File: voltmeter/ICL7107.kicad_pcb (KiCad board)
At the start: 2 copper layers, 88.9 x 68.6 mm, 42 parts, among them J1 +9...12V DC, J2 DP conn., J3 meas. conn, M1 M2.2, M2 M2.2, M3 M2.2, M4 M2.2, U1 LM285Z-1.2, U2 ICL7107, U3 L7805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

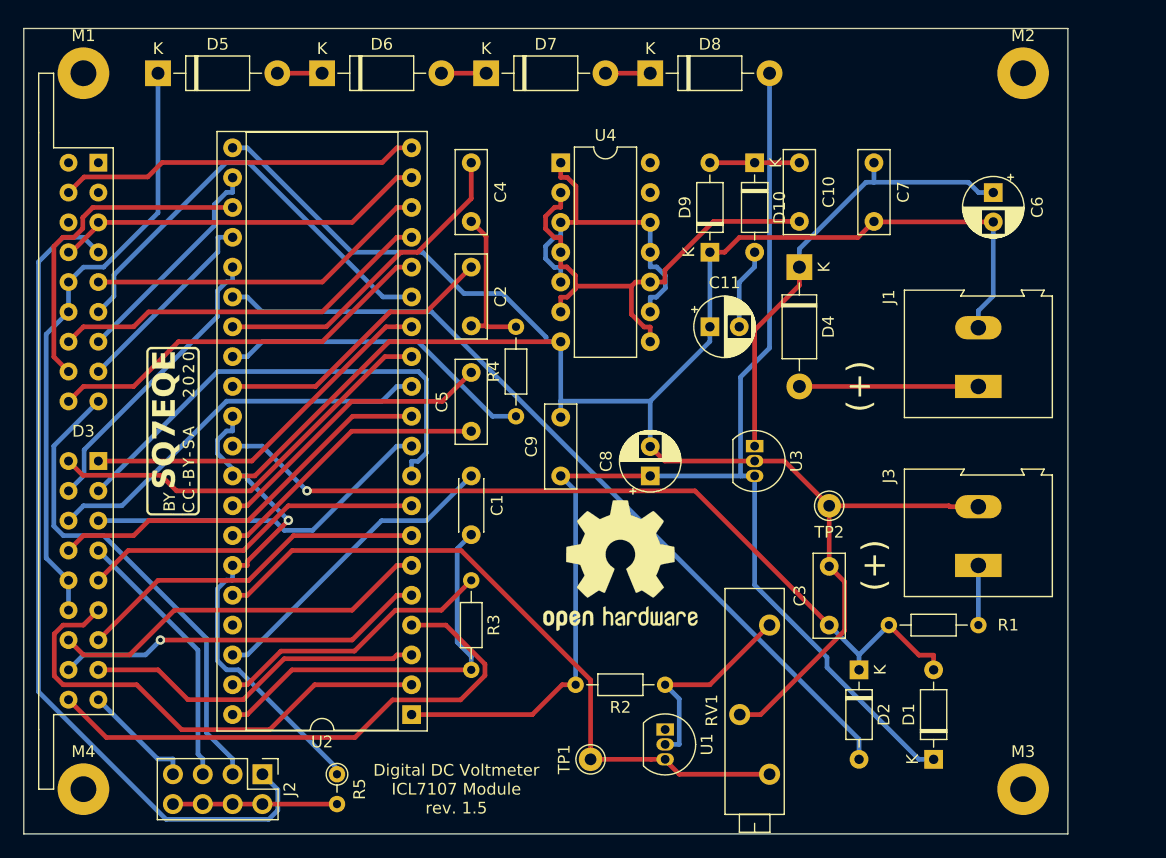
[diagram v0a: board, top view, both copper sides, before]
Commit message: update
I have regenerated Gerber files
I make correction of schematic diagram
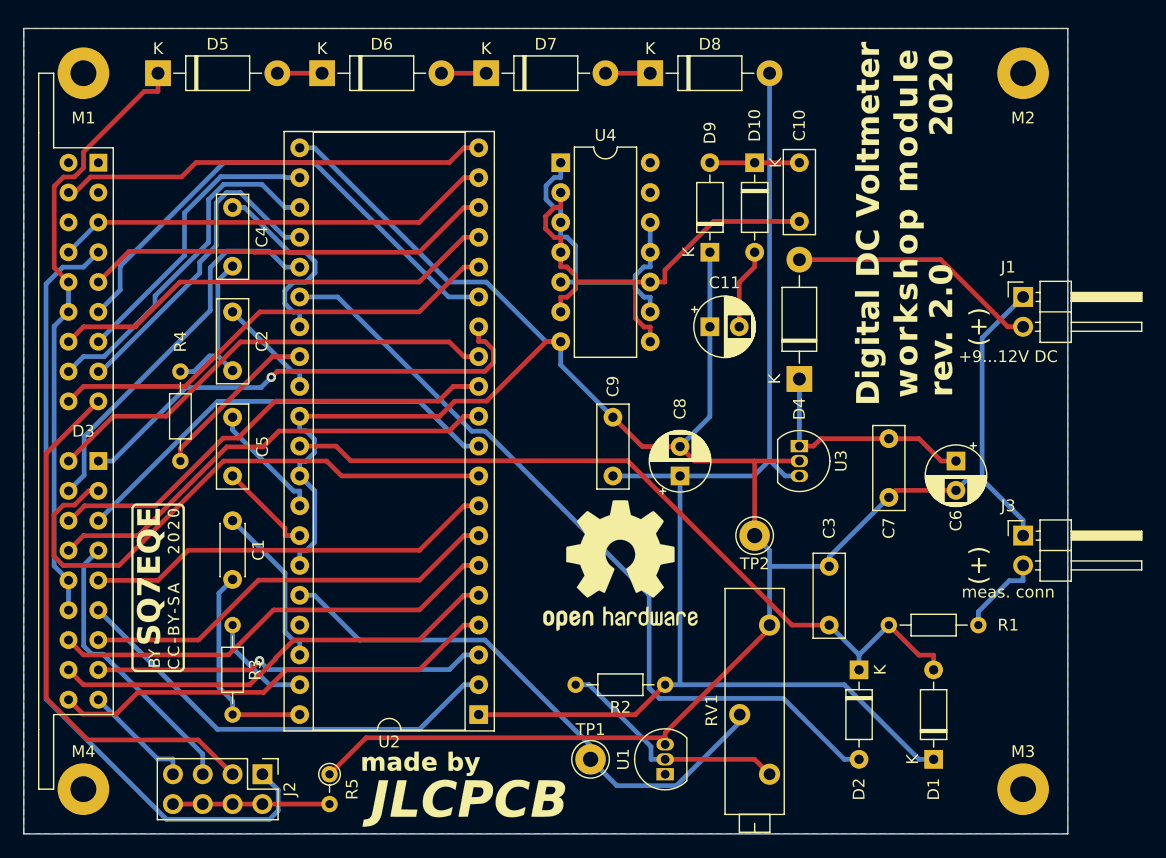
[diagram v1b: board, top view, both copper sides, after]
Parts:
- added #G: DDCVoltmr, logo-sq7eqe:digital-voltmeter-2, F.Cu at (161.3, 76.2)
- added G2: JLCPCB, logo-sq7eqe:jlcpcb, F.Cu at (123.8, 124.5)
- J1, J3: footprint TerminalBlock:TerminalBlock_Altech_AK300-2_P5.00mm -> Connector_PinHeader_2.54mm:PinHeader_1x02_P2.54mm_Horizontal
- TP1, TP2: footprint Connector_Pin:Pin_D1.0mm_L10.0mm -> Connector_Pin:Pin_D1.3mm_L11.0mm
- moved R4 28.8 mm to (99.7, 96.5)
- moved C7 23.5 mm to (160.0, 94.6)
- moved C6 23.1 mm to (165.7, 96.5)
- moved C1 20.7 mm to (104.1, 101.6)
- moved C2 20.7 mm to (104.1, 83.8)
- moved C4 20.7 mm to (104.1, 74.9)
- moved C5 20.7 mm to (104.1, 97.8)
- moved R3 20.7 mm to (104.1, 110.5)
- moved G1 13.4 mm to (97.8, 107.3)
- moved D4 9.52 mm to (152.4, 89.5), turned to 90 degrees
- moved J1 8.52 mm to (171.4, 82.5), turned to 0 degrees
- moved TP2 6.84 mm to (148.6, 102.9)
- moved U2 5.72 mm to (125.1, 118.1)
- moved J3 4.58 mm to (171.4, 102.9), turned to 0 degrees
- moved C9 4.44 mm to (136.5, 97.8)
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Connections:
- J1 pad 1: Net-(D4-Pad2) -> GND
- J1 pad 2: GND -> Net-(D4-Pad2)
- J3 pad 1: /IN+ -> GND
- J3 pad 2: GND -> /IN+
- R2 pad 1: Net-(R2-Pad1) -> /V+
- R2 pad 2: /V+ -> Net-(R2-Pad2)
- RV1 pad 1: Net-(R2-Pad1) -> GND
- RV1 pad 2: GND -> Net-(RV1-Pad2)
- RV1 pad 3: Net-(RV1-Pad3) -> Net-(R2-Pad2)
- TP1 pad 1: Net-(RV1-Pad3) -> Net-(RV1-Pad2)
- U1 pad 2: Net-(R2-Pad1) -> Net-(R2-Pad2)
- U1 pad 3: Net-(RV1-Pad3) -> GND
- U2 pad 36: Net-(RV1-Pad3) -> Net-(RV1-Pad2)
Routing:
- net Net-(RV1-Pad3): track 59.2 -> 0.00 mm
- net Net-(RV1-Pad2): track 0.00 -> 47.8 mm
- net Net-(R2-Pad2): track 0.00 -> 20.3 mm
- net Net-(C6-Pad1): track 39.3 -> 20.1 mm
- net Net-(R2-Pad1): track 17.8 -> 0.00 mm
- net Net-(C1-Pad2): track 34.4 -> 18.2 mm
- net Net-(C5-Pad1): track 24.0 -> 8.18 mm
- net Net-(C2-Pad1): track 24.5 -> 9.08 mm
- net GND: track 231.2 -> 216.0 mm, vias 1 -> 0
- net Net-(R3-Pad1): track 24.0 -> 8.96 mm
- net Net-(C5-Pad2): track 25.0 -> 10.2 mm
- net Net-(R4-Pad1): track 27.3 -> 14.5 mm
- net /OSC3: track 26.6 -> 14.1 mm
- net Net-(C4-Pad1): track 27.9 -> 17.0 mm
- net Net-(D3-Pad8): track 16.9 -> 27.7 mm
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- added copper zone on B.Cu, net GND
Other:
- board text removed: "Digital DC Voltmeter ICL7107 Module rev. 1.5"

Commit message: upload modified file
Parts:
- U3: footprint Package_TO_SOT_THT:TO-92_Inline -> Package_TO_SOT_THT:TO-220-3_Vertical
- moved U3 5.68 mm to (154.9, 100.3), turned to 90 degrees
- moved TP2 4.02 mm to (144.8, 104.1)
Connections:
- C1 pad 1: /OSC3 -> OSC3
- C11 pad 2: /negative voltage converter/V- -> -5V
- C8 pad 1: /V+ -> +5V
- C9 pad 1: /V+ -> +5V
- D1 pad 1: /V+ -> +5V
- D10 pad 2: /negative voltage converter/V- -> -5V
- D2 pad 2: /V- -> -5V
- D8 pad 2: /V+ -> +5V
- R2 pad 1: /V+ -> +5V
- U2 pad 1: /V+ -> +5V
- U2 pad 26: /V- -> -5V
- U2 pad 38: /OSC3 -> OSC3
- U3 pad 3: /V+ -> +5V
- U4 pad 13: /negative voltage converter/OSC3 -> OSC3
- U4 pad 14: /negative voltage converter/V+ -> +5V
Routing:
- net +5V: track 0.00 -> 121.6 mm
- net /V+: track 110.1 -> 0.00 mm
- net -5V: track 0.00 -> 93.1 mm
- net /V-: track 68.6 -> 0.00 mm
- net OSC3: track 0.00 -> 65.2 mm
- net Net-(D3-Pad30): track 38.6 -> 80.7 mm
- net /DP4: track 68.9 -> 52.1 mm
- net /OSC3: track 14.1 -> 0.00 mm
- net Net-(D3-Pad35): track 32.8 -> 43.6 mm, vias 0 -> 1
- net Net-(D3-Pad12): track 38.6 -> 49.2 mm, vias 0 -> 1
- net GND: track 216.0 -> 206.8 mm
- net /DP3: track 45.7 -> 36.5 mm
- net Net-(RV1-Pad2): track 47.8 -> 55.6 mm
- net Net-(D3-Pad24): track 38.2 -> 45.7 mm
- net /negative voltage converter/V-: track 6.89 -> 0.00 mm
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- added copper zone on F.Cu, net GND
- removed copper zone on B.Cu, net GND
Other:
- net class +5V added: clearance 0.25, trace_width 0.8, via_dia 0.8, via_drill 0.4
